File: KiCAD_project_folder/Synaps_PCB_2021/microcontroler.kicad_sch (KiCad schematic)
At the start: 27 parts, among them IC2 ESP32-S2, Y2 Crystal_GND24

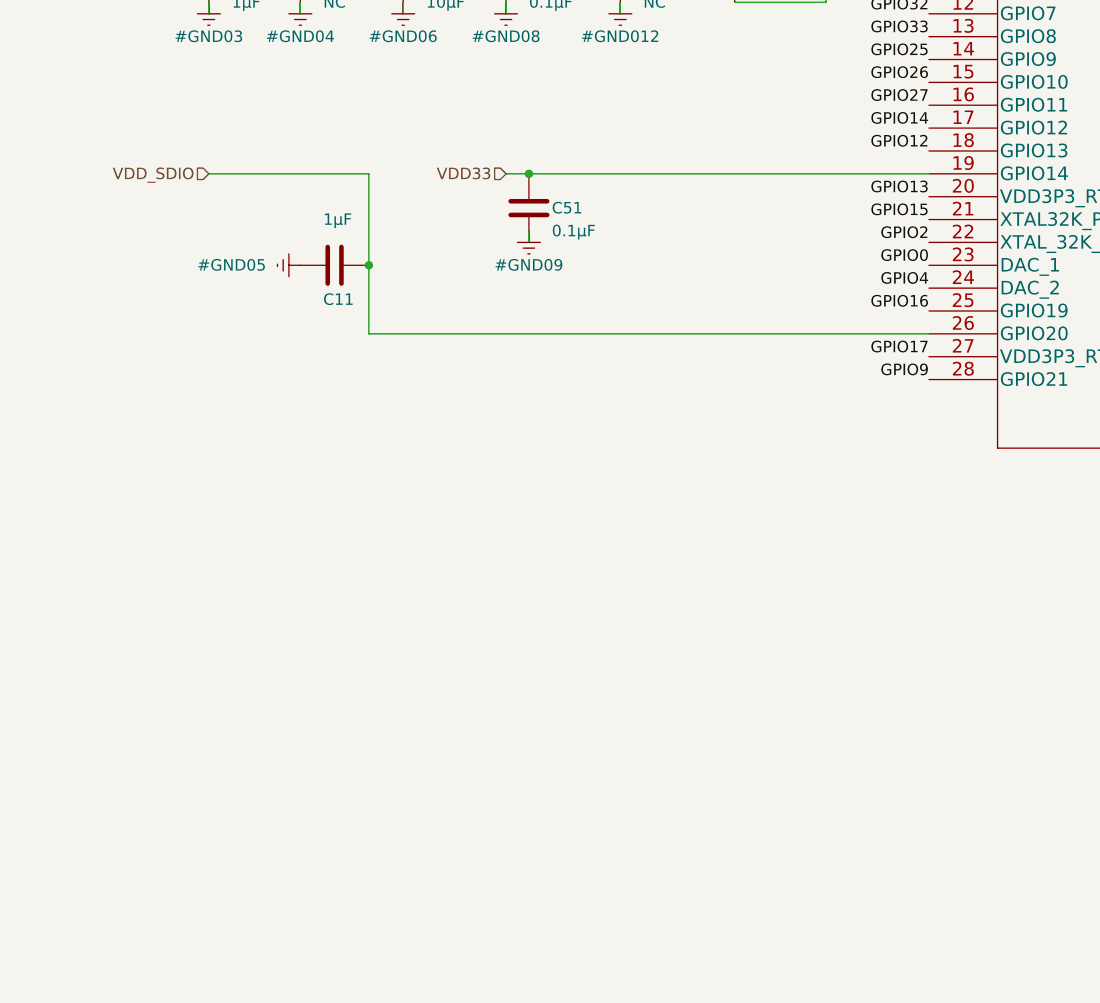
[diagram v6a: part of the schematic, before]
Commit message: Reworking Powersupply
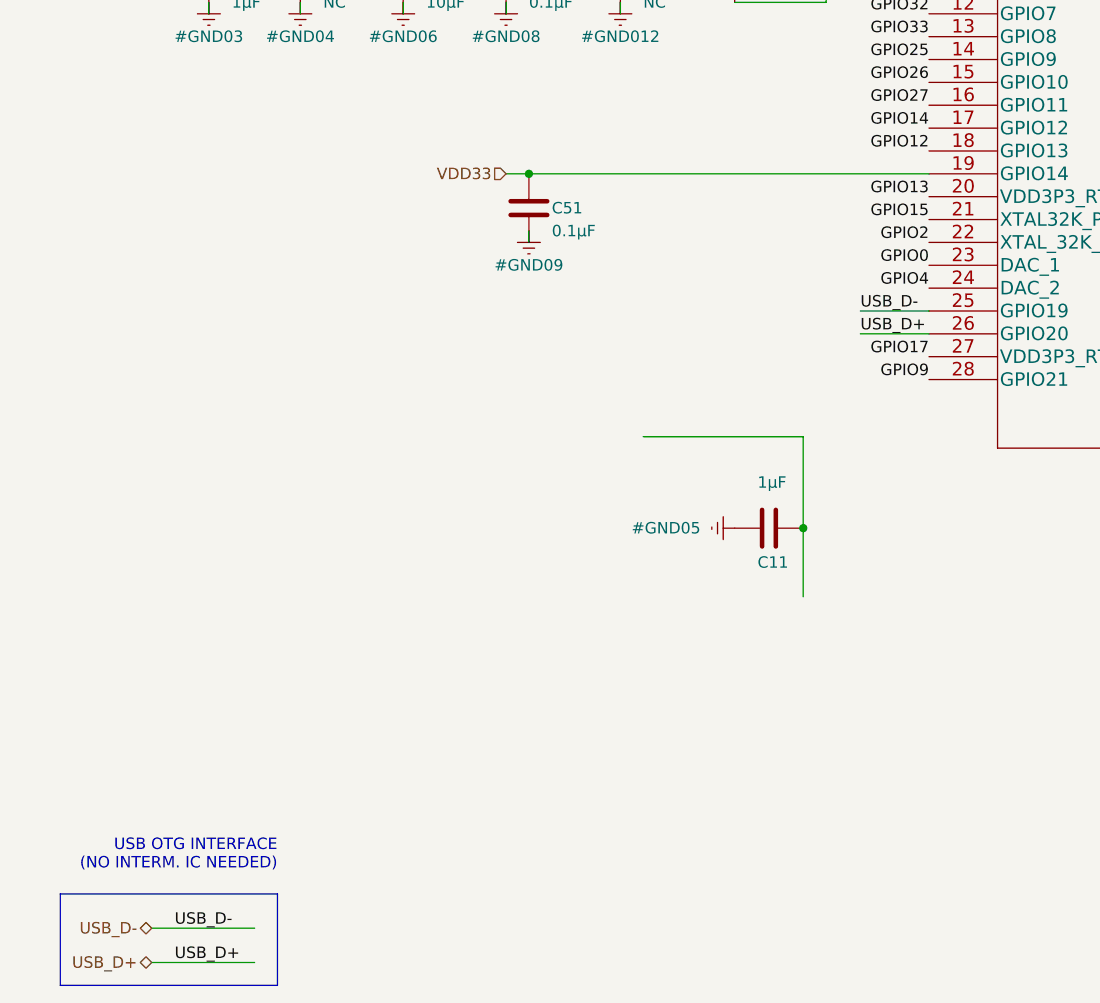
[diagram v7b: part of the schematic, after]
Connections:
- net GPIO16 renamed USB_D-
- net VDD_SDIO: no longer names the net of C11.1
- net VDD_SDIO: no longer IC2.26 (GPIO20)
- new net USB_D+: IC2.26 (GPIO20)
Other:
- note added: "USB OTG INTERFACE (NO INTERM. IC NEEDED)"
- moved on the sheet: C11
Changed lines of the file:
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@@
   (junction (at 226.06 114.3) (diameter 0) (color 0 0 0 0)
   )
-  (junction (at 48.26 115.57) (diameter 0) (color 0 0 0 0)
+  (junction (at 96.52 144.78) (diameter 0) (color 0 0 0 0)
   )
   (junction (at 63.5 80.01) (diameter 0) (color 0 0 0 0)
@@
     (stroke (width 0) (type default) (color 0 0 0 0))
   )
+  (polyline (pts (xy 13.97 185.42) (xy 13.97 195.58))
+    (stroke (width 0) (type default) (color 0 0 0 0))
+  )
   (wire (pts (xy 181.61 95.25) (xy 208.28 95.25))
     (stroke (width 0) (type default) (color 0 0 0 0))
@@
     (stroke (width 0) (type default) (color 0 0 0 0))
   )
+  (polyline (pts (xy 38.1 185.42) (xy 38.1 195.58))
+    (stroke (width 0) (type default) (color 0 0 0 0))
+  )
   (wire (pts (xy 66.04 113.03) (xy 66.04 111.76))
     (stroke (width 0) (type default) (color 0 0 0 0))
@@
     (stroke (width 0) (type default) (color 0 0 0 0))
   )
-  (wire (pts (xy 30.48 105.41) (xy 48.26 105.41))
-    (stroke (width 0) (type default) (color 0 0 0 0))
-  )
-  (wire (pts (xy 48.26 115.57) (xy 48.26 105.41))
+  (wire (pts (xy 78.74 134.62) (xy 96.52 134.62))
+    (stroke (width 0) (type default) (color 0 0 0 0))
+  )
+  (wire (pts (xy 96.52 144.78) (xy 96.52 134.62))
     (stroke (width 0) (type default) (color 0 0 0 0))
   )
@@
     (stroke (width 0) (type default) (color 0 0 0 0))
   )
+  (wire (pts (xy 102.87 123.19) (xy 110.49 123.19))
+    (stroke (width 0) (type default) (color 0 0 0 0))
+  )
   (wire (pts (xy 205.74 114.3) (xy 226.06 114.3))
     (stroke (width 0) (type default) (color 0 0 0 0))
   )
+  (polyline (pts (xy 13.97 185.42) (xy 38.1 185.42))
+    (stroke (width 0) (type default) (color 0 0 0 0))
+  )
   (wire (pts (xy 97.79 74.93) (xy 97.79 78.74))
     (stroke (width 0) (type default) (color 0 0 0 0))
@@
     (stroke (width 0) (type default) (color 0 0 0 0))
   )
+  (wire (pts (xy 24.13 189.23) (xy 35.56 189.23))
+    (stroke (width 0) (type default) (color 0 0 0 0))
+  )
   (wire (pts (xy 195.58 110.49) (xy 195.58 148.59))
     (stroke (width 0) (type default) (color 0 0 0 0))
@@
     (stroke (width 0) (type default) (color 0 0 0 0))
   )
+  (polyline (pts (xy 38.1 195.58) (xy 13.97 195.58))
+    (stroke (width 0) (type default) (color 0 0 0 0))
+  )
   (wire (pts (xy 40.64 44.45) (xy 58.42 44.45))
     (stroke (width 0) (type default) (color 0 0 0 0))
@@
     (stroke (width 0) (type default) (color 0 0 0 0))
   )
-  (wire (pts (xy 110.49 123.19) (xy 48.26 123.19))
-    (stroke (width 0) (type default) (color 0 0 0 0))
-  )
   (wire (pts (xy 96.52 72.39) (xy 96.52 77.47))
     (stroke (width 0) (type default) (color 0 0 0 0))
@@
     (stroke (width 0) (type default) (color 0 0 0 0))
   )
+  (wire (pts (xy 24.13 193.04) (xy 35.56 193.04))
+    (stroke (width 0) (type default) (color 0 0 0 0))
+  )
   (wire (pts (xy 227.33 102.87) (xy 227.33 101.6))
     (stroke (width 0) (type default) (color 0 0 0 0))
@@
     (stroke (width 0) (type default) (color 0 0 0 0))
   )
+  (wire (pts (xy 102.87 120.65) (xy 110.49 120.65))
+    (stroke (width 0) (type default) (color 0 0 0 0))
+  )
   (wire (pts (xy 66.04 105.41) (xy 110.49 105.41))
     (stroke (width 0) (type default) (color 0 0 0 0))
@@
     (stroke (width 0) (type default) (color 0 0 0 0))
   )
-  (wire (pts (xy 48.26 123.19) (xy 48.26 115.57))
+  (wire (pts (xy 96.52 152.4) (xy 96.52 144.78))
     (stroke (width 0) (type default) (color 0 0 0 0))
   )
@@
     (stroke (width 0) (type default) (color 0 0 0 0))
   )
+  (text "USB OTG INTERFACE\n(NO INTERM. IC NEEDED)" (at 38.1 182.88 180)
+    (effects (font (size 1.27 1.27)) (justify right bottom))
+  )
   (label "GPIO11" (at 181.61 128.27 0)
     (effects (font (size 1.27 1.27)) (justify left bottom))
@@
     (effects (font (size 1.27 1.27)) (justify right bottom))
   )
-  (label "GPIO16" (at 110.49 120.65 180)
-    (effects (font (size 1.27 1.27)) (justify right bottom))
-  )
   (label "SENSOR_VN" (at 101.6 77.47 0)
     (effects (font (size 1.27 1.27)) (justify left bottom))
@@
     (effects (font (size 1.27 1.27)) (justify right bottom))
   )
+  (label "USB_D-" (at 26.67 189.23 0)
+    (effects (font (size 1.27 1.27)) (justify left bottom))
+  )
   (label "GPIO1" (at 200.66 106.68 270)
     (effects (font (size 1.27 1.27)) (justify right bottom))
@@
     (effects (font (size 1.27 1.27)) (justify right bottom))
   )
+  (label "USB_D+" (at 102.87 123.19 0)
+    (effects (font (size 1.27 1.27)) (justify left bottom))
+  )
   (label "GPIO23" (at 181.61 113.03 0)
     (effects (font (size 1.27 1.27)) (justify left bottom))
@@
   (label "GPIO33" (at 110.49 90.17 180)
     (effects (font (size 1.27 1.27)) (justify right bottom))
+  )
+  (label "USB_D-" (at 102.87 120.65 0)
+    (effects (font (size 1.27 1.27)) (justify left bottom))
+  )
+  (label "USB_D+" (at 26.67 193.04 0)
+    (effects (font (size 1.27 1.27)) (justify left bottom))
   )
   (label "GPIO15" (at 110.49 110.49 180)
@@
     (effects (font (size 1.27 1.27)) (justify right))
   )
+  (hierarchical_label "USB_D+" (shape bidirectional) (at 24.13 193.04 180)
+    (effects (font (size 1.27 1.27)) (justify right))
+  )
   (hierarchical_label "VDD33" (shape input) (at 63.5 105.41 180)
     (effects (font (size 1.27 1.27)) (justify right))
   )
-  (hierarchical_label "VDD_SDIO" (shape input) (at 30.48 105.41 180)
+  (hierarchical_label "USB_D-" (shape bidirectional) (at 24.13 189.23 180)
     (effects (font (size 1.27 1.27)) (justify right))
   )
@@
     (pin "1")
   )
-  (symbol (lib_id "Device:C") (at 44.45 115.57 270) (unit 1)
-    (in_bom yes) (on_board yes)
-    (property "Reference" "C11" (id 0) (at 43.18 119.38 90)
-      (effects (font (size 1.27 1.27)) (justify left))
-    )
-    (property "Value" "1µF" (id 1) (at 43.18 110.49 90)
-      (effects (font (size 1.27 1.27)) (justify left))
-    )
-    (property "Footprint" "Capacitor_SMD:C_1206_3216Metric_Pad1.33x1.80mm_HandSolder" (id 2) (at 40.64 116.5352 0)
-      (effects (font (size 1.27 1.27)) hide)
-    )
-    (property "Datasheet" "~" (id 3) (at 44.45 115.57 0)
+  (symbol (lib_id "Device:C") (at 92.71 144.78 270) (unit 1)
+    (in_bom yes) (on_board yes)
+    (property "Reference" "C11" (id 0) (at 91.44 148.59 90)
+      (effects (font (size 1.27 1.27)) (justify left))
+    )
+    (property "Value" "1µF" (id 1) (at 91.44 139.7 90)
+      (effects (font (size 1.27 1.27)) (justify left))
+    )
+    (property "Footprint" "Capacitor_SMD:C_1206_3216Metric_Pad1.33x1.80mm_HandSolder" (id 2) (at 88.9 145.7452 0)
+      (effects (font (size 1.27 1.27)) hide)
+    )
+    (property "Datasheet" "~" (id 3) (at 92.71 144.78 0)
       (effects (font (size 1.27 1.27)) hide)
     )
@@
     (pin "1")
   )
-  (symbol (lib_id "power:Earth") (at 40.64 115.57 270) (unit 1)
-    (in_bom yes) (on_board yes)
-    (property "Reference" "#GND05" (id 0) (at 33.02 115.57 90))
-    (property "Value" "Earth" (id 1) (at 36.83 115.57 0)
-      (effects (font (size 1.27 1.27)) hide)
-    )
-    (property "Footprint" "" (id 2) (at 40.64 115.57 0)
-      (effects (font (size 1.27 1.27)) hide)
-    )
-    (property "Datasheet" "~" (id 3) (at 40.64 115.57 0)
-      (effects (font (size 1.27 1.27)) hide)
-    )
+  (symbol (lib_id "power:Earth") (at 88.9 144.78 270) (unit 1)
+    (in_bom yes) (on_board yes)
+    (property "Reference" "#GND05" (id 0) (at 81.28 144.78 90))
+    (property "Value" "Earth" (id 1) (at 85.09 144.78 0)
+      (effects (font (size 1.27 1.27)) hide)
+    )
+    (property "Footprint" "" (id 2) (at 88.9 144.78 0)
+      (effects (font (size 1.27 1.27)) hide)
+    )
+    (property "Datasheet" "~" (id 3) (at 88.9 144.78 0)
+      (effects (font (size 1.27 1.27)) hide)
+    )
